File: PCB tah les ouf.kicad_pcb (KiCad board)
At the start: 2 copper layers, 60 x 60 mm, 14 parts, among them J1 USB_C_Receptacle_USB2.0_16P, Q1 2N7002, Q2 2N7002, U1 ESP32-S3-WROOM-1, U2 TMC2209_SILENTSTEPSTICK, U3 TMC2209_SILENTSTEPSTICK, U4 TMC2209_SILENTSTEPSTICK, U5 TMC2209_SILENTSTEPSTICK, U6 D3V3XA4B10LP, U7 AMS1117-3.3, U8 CH340C

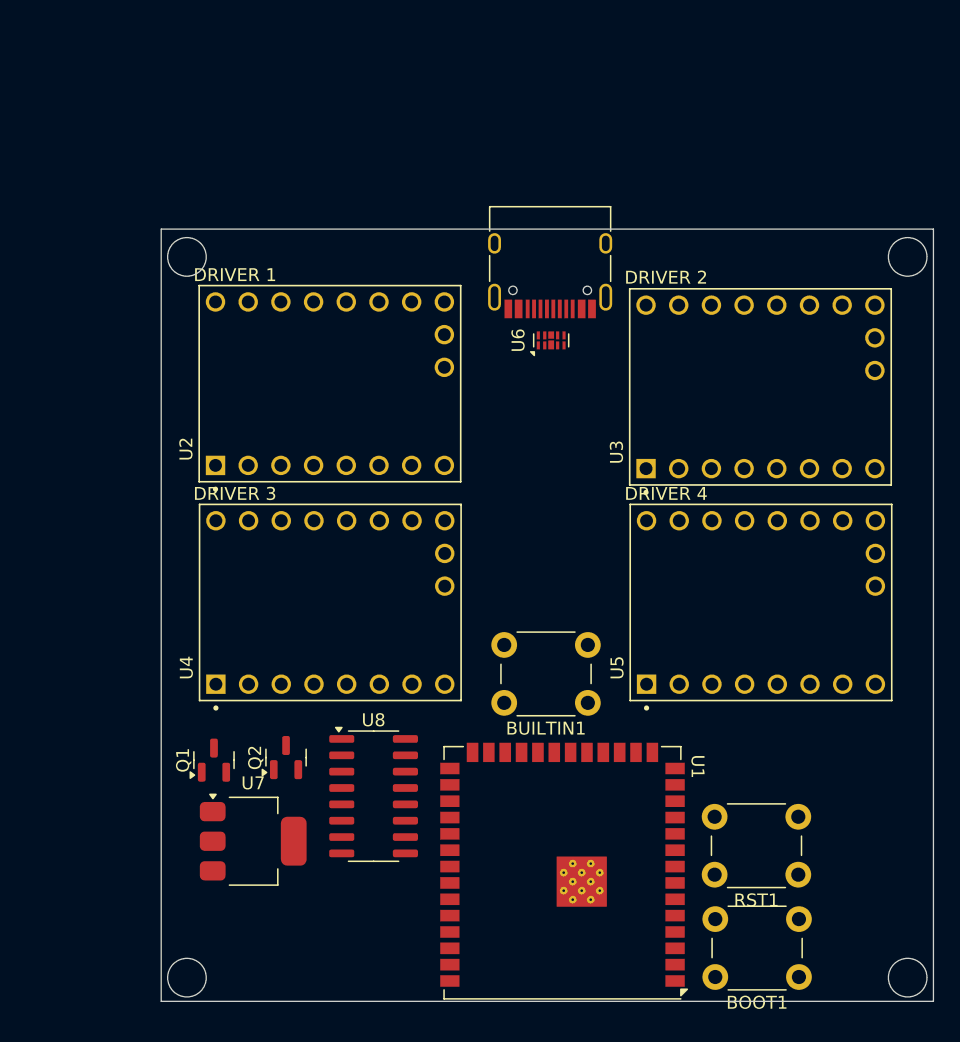
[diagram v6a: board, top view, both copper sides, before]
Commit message: auto flash mode v2
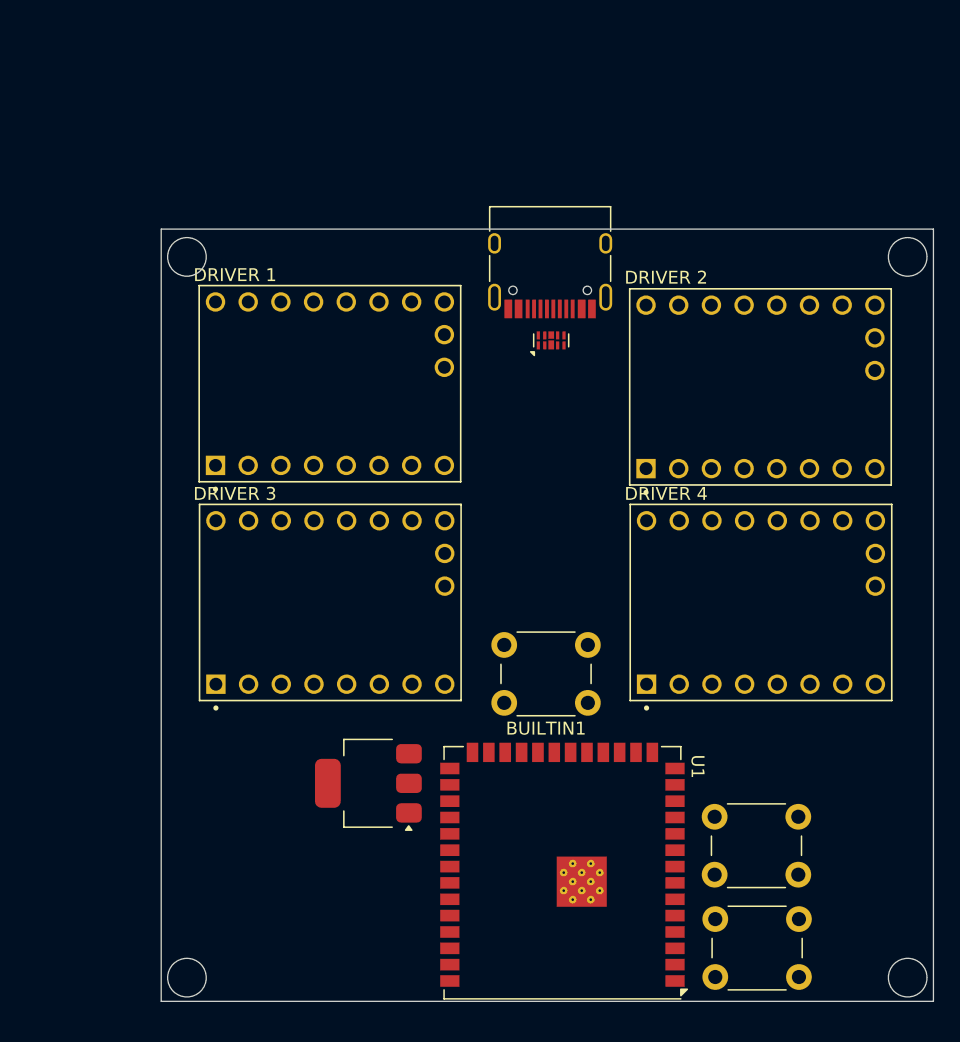
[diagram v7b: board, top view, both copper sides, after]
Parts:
- removed Q1, Q2: 2N7002, Package_TO_SOT_SMD:SOT-23
- removed U8: CH340C, Package_SO:SOIC-16_3.9x9.9mm_P1.27mm
- moved U7 10.0 mm to (115.6, 102.9), turned to 180 degrees

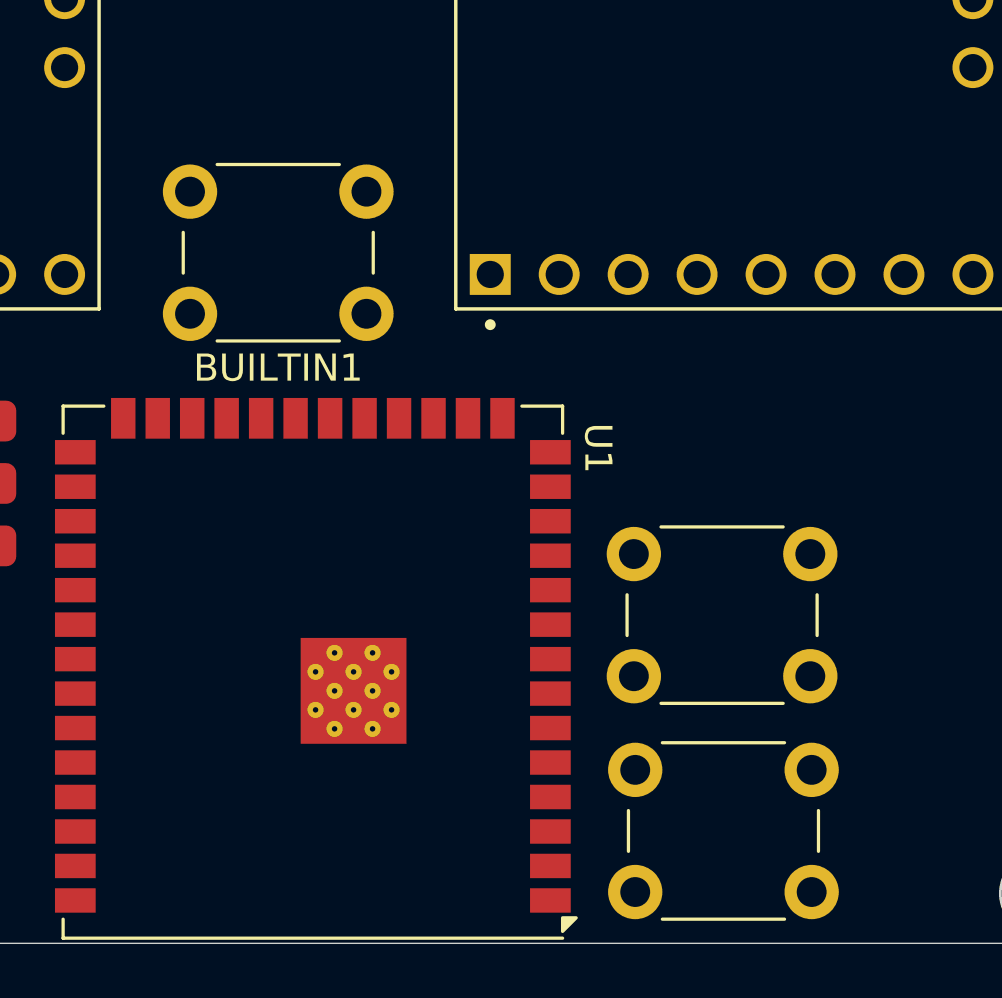
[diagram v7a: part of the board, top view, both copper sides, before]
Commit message: Add buttons for reset, boot, and built-in functions
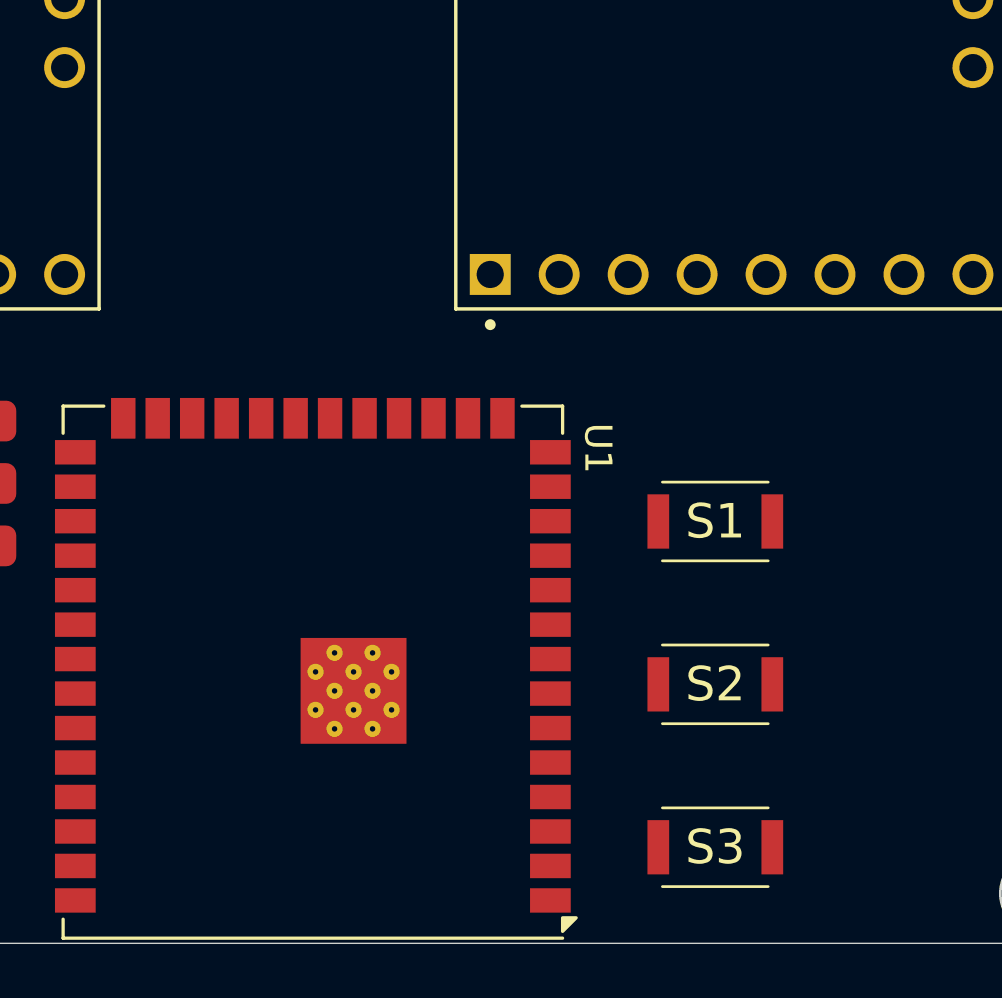
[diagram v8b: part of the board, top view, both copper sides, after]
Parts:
- removed BOOT1, BUILTIN1, RST1: SW_MEC_5E, Button_Switch_THT:SW_PUSH_6mm_H4.3mm
- added S1: BOOT, Bouton:SKRKAEE020, F.Cu at (145.5, 104.3)
- added S2: RST, Bouton:SKRKAEE020, F.Cu at (145.5, 110.3)
- added S3: BUILTIN, Bouton:SKRKAEE020, F.Cu at (145.5, 116.3)
- U7: value AMS1117-3.3 -> AMS1117-3.3 (UMW)
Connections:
- U2 pad 14: unconnected-(U2-MS2-Pad14) -> Net-(U2-MS2)
- U2 pad 15: unconnected-(U2-MS1-Pad15) -> Net-(U2-MS1)
- U2 pad 2: unconnected-(U2-VIO-Pad2) -> Net-(U2-VIO)
- U3 pad 14: unconnected-(U3-MS2-Pad14) -> Net-(U3-MS2)
- U3 pad 15: unconnected-(U3-MS1-Pad15) -> Net-(U3-MS1)
- U3 pad 2: unconnected-(U3-VIO-Pad2) -> Net-(U3-VIO)
- U4 pad 14: unconnected-(U4-MS2-Pad14) -> Net-(U4-MS2)
- U4 pad 15: unconnected-(U4-MS1-Pad15) -> Net-(U4-MS1)
- U4 pad 2: unconnected-(U4-VIO-Pad2) -> Net-(U4-VIO)
- U5 pad 14: unconnected-(U5-MS2-Pad14) -> Net-(U5-MS2)
- U5 pad 15: unconnected-(U5-MS1-Pad15) -> Net-(U5-MS1)
- U5 pad 2: unconnected-(U5-VIO-Pad2) -> Net-(U5-VIO)
- U7 pad 1: unconnected-(U7-GND-Pad1) -> GND
- U7 pad 2: unconnected-(U7-VO-Pad2) -> /3V3
- U7 pad 3: unconnected-(U7-VI-Pad3) -> /VCC_5V
